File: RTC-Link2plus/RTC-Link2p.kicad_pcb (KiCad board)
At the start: 2 copper layers, 60 x 71.9 mm, 17 parts, among them CN1 EDGE_CON_02x12, J1 Conn_02x07_Odd_Even, J2 Flyout1, J3 Flyout2, J4 Conn_01x03, P1 c64cartedge, U1 MC68A21, U2 74LS30, U3 74LS00, U5 27C512PLCC

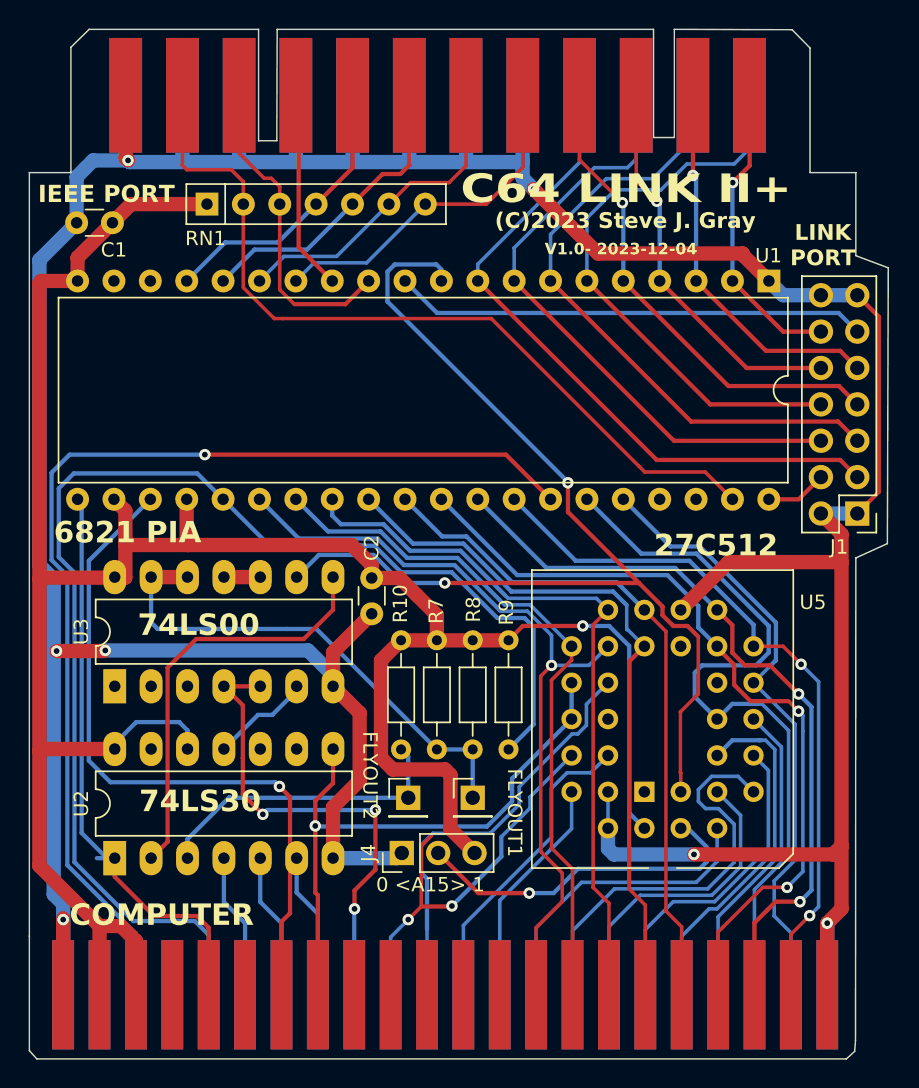
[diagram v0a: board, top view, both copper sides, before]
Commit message: Update to Kicad 9. Add Gerbers, component values, iBom
Update files to Kicad 9 format. Add Gerbers. Add more component values. Generate interactive BOM.  Boards have been made but not tested. Use at own risk!
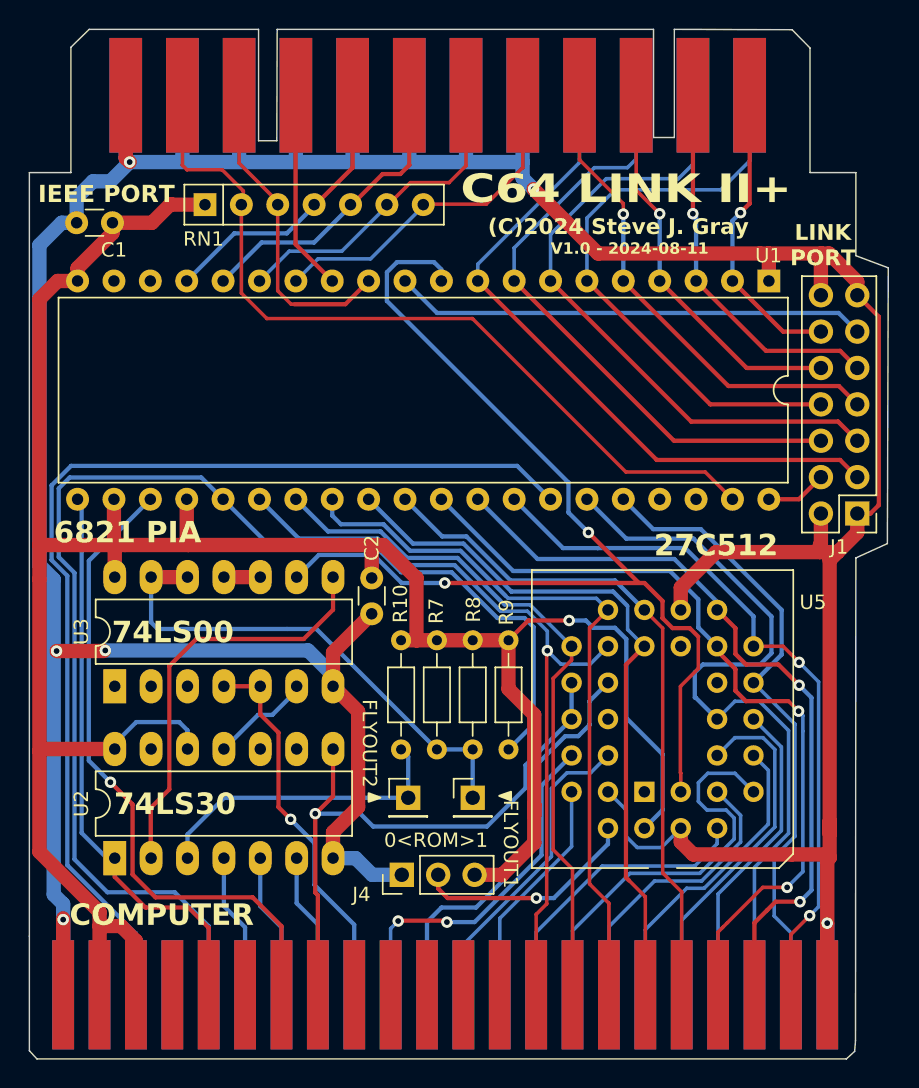
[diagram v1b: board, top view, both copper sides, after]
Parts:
- C1, C2: value C -> 0.1uf
- J4: value Conn_01x03 -> A13
- R10, R7, R8, R9: value R -> 10K
- RN1: value R_Network06 -> 10K
- moved J4 1.52 mm to (149.3, 104.6)
- moved RN1 0.14 mm to (135.6, 57.8)
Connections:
- U5 pad 2: Net-(J4-Pin_2) -> GND
- U5 pad 30: GND -> Net-(J4-Pin_2)
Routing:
- net Net-(J4-Pin_2): track 24.2 -> 15.8 mm
- net GND: track 302.4 -> 310.2 mm, vias 7 -> 6
- net A12: track 34.1 -> 26.8 mm, vias 3 -> 1
- net ~{IO1}: track 49.2 -> 45.9 mm
- net A11: track 28.4 -> 25.2 mm
- net 5V: track 177.6 -> 180.3 mm
- net R/~{W}: track 41.2 -> 40.0 mm
- net ~{RESET}: track 75.6 -> 74.4 mm, vias 1 -> 0
- net A0: track 43.1 -> 44.2 mm
- net PA5: track 45.0 -> 46.1 mm
- net A5: track 21.6 -> 20.6 mm
- net A4: track 22.4 -> 21.4 mm
- net A10: track 29.9 -> 29.0 mm
- net A1: track 53.5 -> 54.5 mm
- net A7: track 21.5 -> 20.6 mm
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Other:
- board text added: "(C)2024 Steve J. Gray"
- board text added: "0<ROM>1"
- board text added: "V1.0 - 2024-08-11"
- board text removed: "(C)2023 Steve J. Gray"
- board text removed: "0 <A15> 1"
- board text removed: "V1.0- 2023-12-04"
